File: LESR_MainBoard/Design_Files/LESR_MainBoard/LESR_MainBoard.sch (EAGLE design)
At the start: 39 parts, among them J1 DCJ0202, Q1 SS8050-G, Q2 SS8050-G, U1 TCA9548APWR, U2 NCP1117ST33T3G, U3 ESP32-WROOM-32, U4 CP2102N-A01-GQFN28, U5 SP0503BAHT

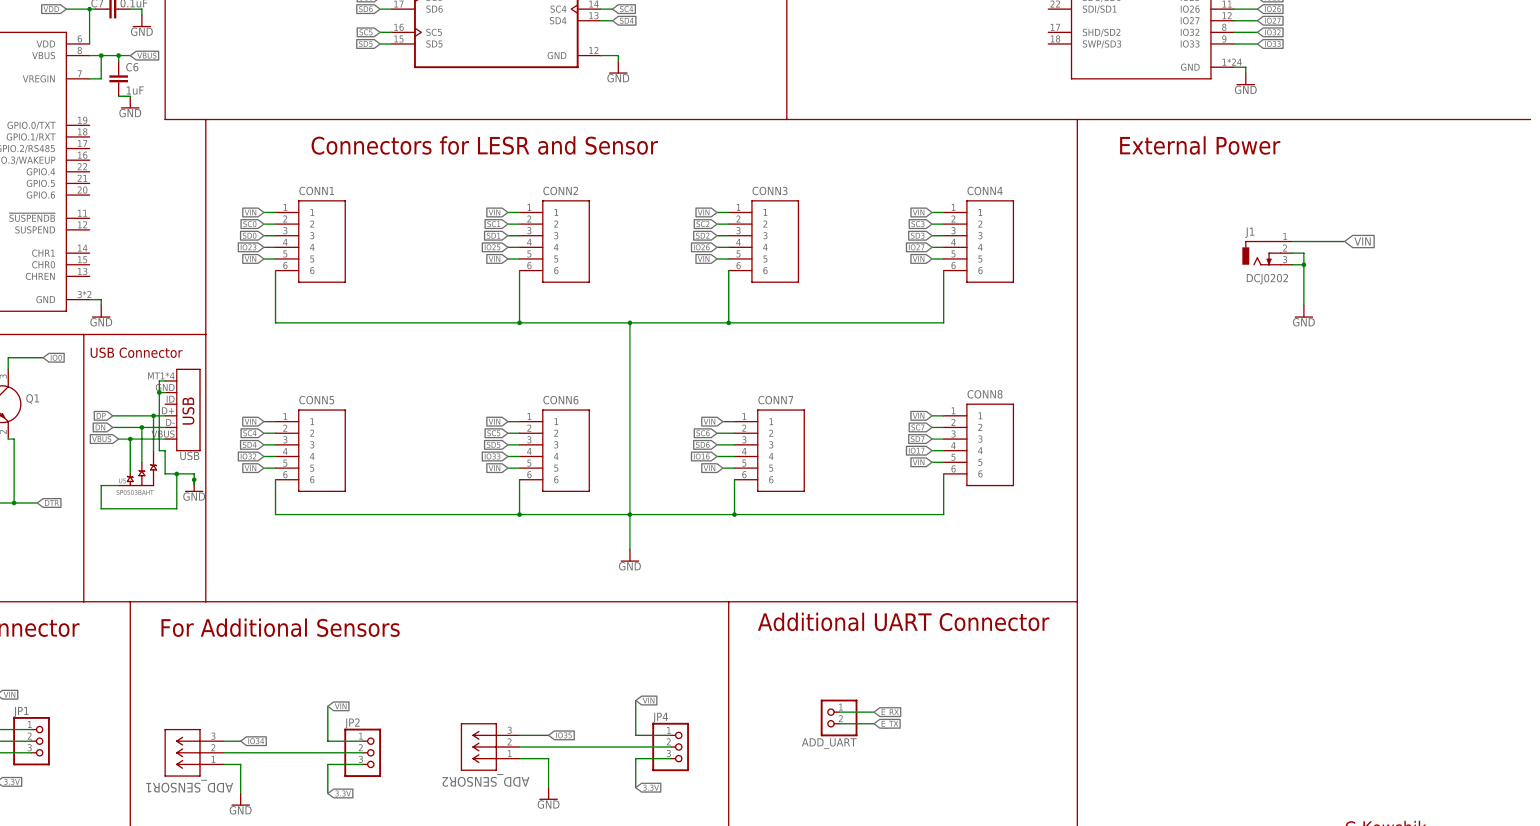
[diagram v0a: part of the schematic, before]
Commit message: 12V to 5V LDO version
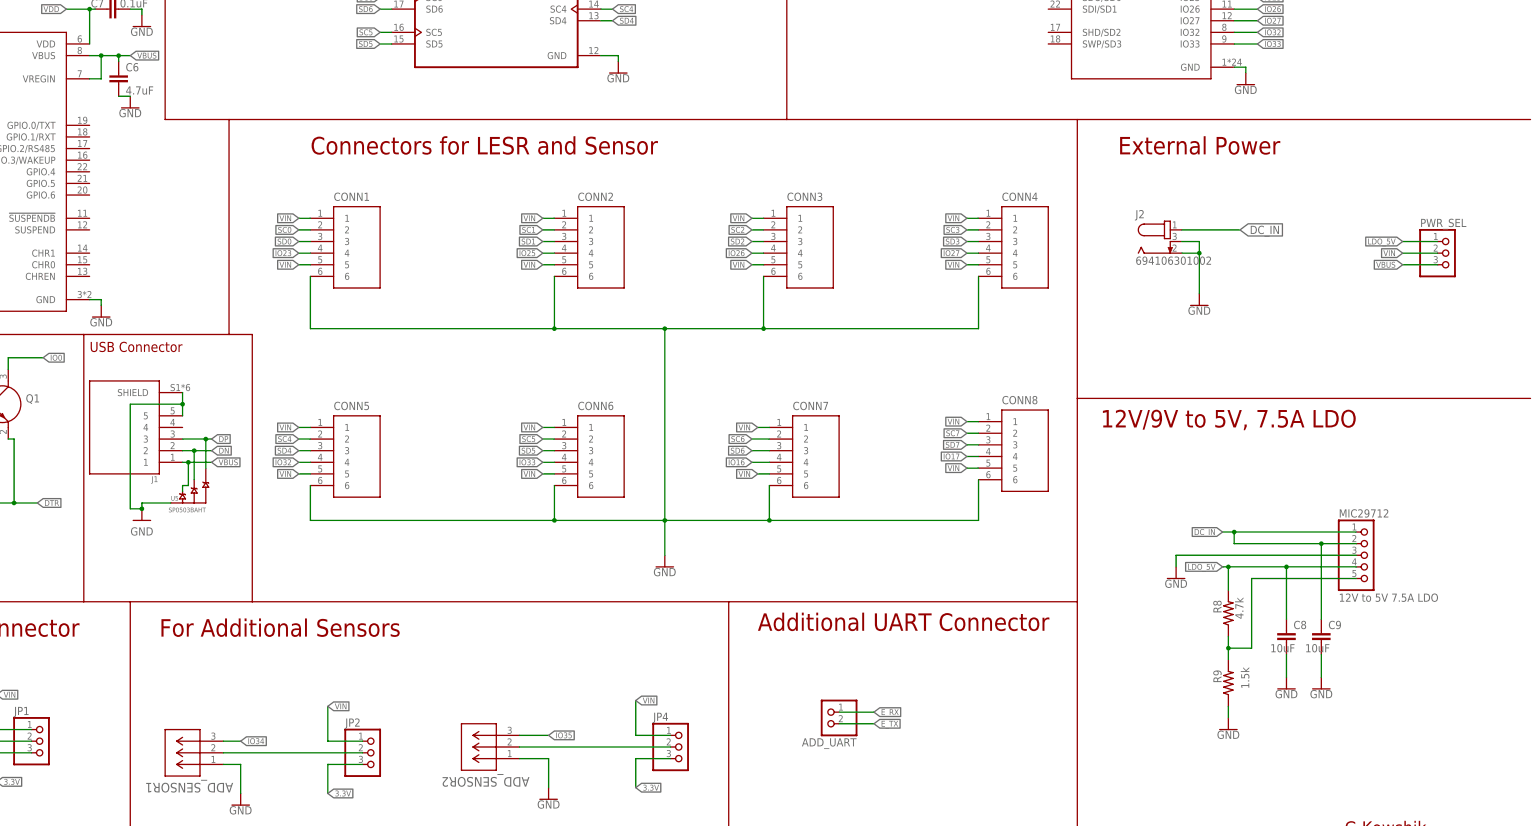
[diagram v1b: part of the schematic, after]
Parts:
- removed USB: (no value), SparkFun-Connectors:USB_MICRO-B_SMT
- added C8, C9: 10uF, rcl:C-EUC0805
- added J2: 694106301002, DC Power Jacks:694106301002
- added MIC29712: 12V to 5V 7.5A LDO, pinhead:PINHD-1X5
- added PWR_SEL: (no value), adafruit:PINHD-1X3
- added R8: 4.7k, rcl:R-US_R0805
- added R9: 1.5k, rcl:R-US_R0805
- C6: value 1uF -> 4.7uF
- J1: value DCJ0202 -> 10118194-0001LF; device con-jack:DCJ0202 -> ThHole-USB-Micro-BType-receptacle:10118194-0001LF
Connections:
- new net DC_IN: C9.1, J2.1, MIC29712.1, MIC29712.2
- new net LDO_5V: C8.1, MIC29712.4, PWR_SEL.1, R8.2
- new net N$2: MIC29712.5, R8.1, R9.2
- net DN: now also J1.2; no longer USB.D-
- net DP: now also J1.3; no longer USB.D+
- net GND: now also C8.2, C9.2, J1.5, J1.SHIELD, J2.2, J2.3, MIC29712.3, R9.1; no longer J1.2, J1.3, USB.GND, USB.SHIELD
- net VBUS: now also J1.1, PWR_SEL.3; no longer USB.VBUS
- net VIN: now also PWR_SEL.2; no longer J1.1
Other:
- note added: "12V/9V to 5V, 7.5A LDO"
- moved on the sheet: CONN1, CONN2, CONN3, CONN4, CONN5, CONN6, CONN7, CONN8, U5

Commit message: Controller dimensions changed
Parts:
- MIC29712: value 12V to 5V 7.5A LDO -> MIC29712WT; device pinhead:PINHD-1X5 -> MIC29712WT:MIC29712WT
- renumbered J1 to USB
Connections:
- net DC_IN: now also MIC29712.EN, MIC29712.IN; no longer MIC29712.1, MIC29712.2
- net GND: now also MIC29712.GND; no longer MIC29712.3
- net LDO_5V: now also MIC29712.OUT; no longer MIC29712.4
- net N$2: now also MIC29712.ADJ; no longer MIC29712.5
